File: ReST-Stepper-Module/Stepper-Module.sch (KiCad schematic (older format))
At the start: 13 parts, among them P1 CONN_02X10, P2 CONN_01X04, P3 CONN_01X04, P4 CONN_01X04, P5 CONN_01X04, P6 CONN_02X03, P7 CONN_02X03, U1 POLOLU_A4988, U2 POLOLU_A4988

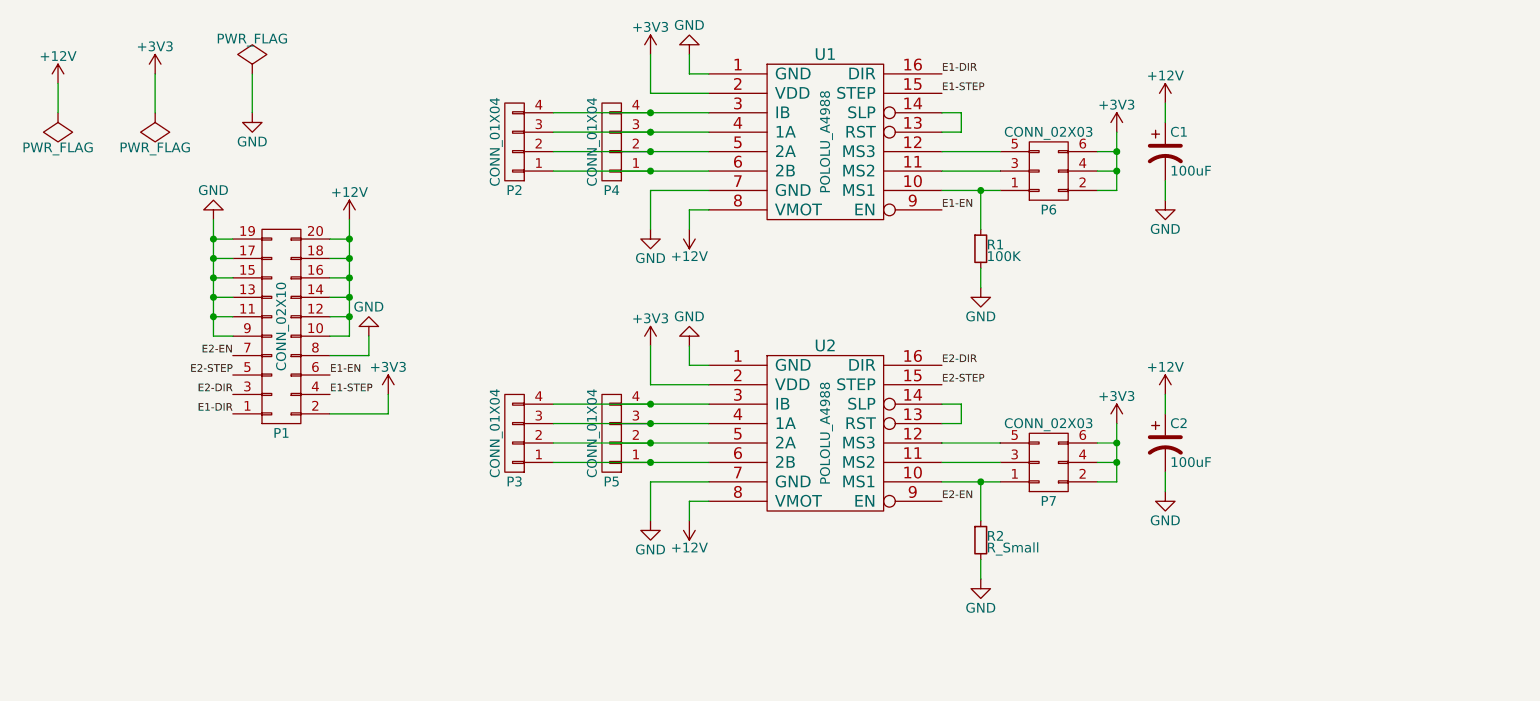
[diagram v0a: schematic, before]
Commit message: Added Images and PDF's
+ Silkscreening
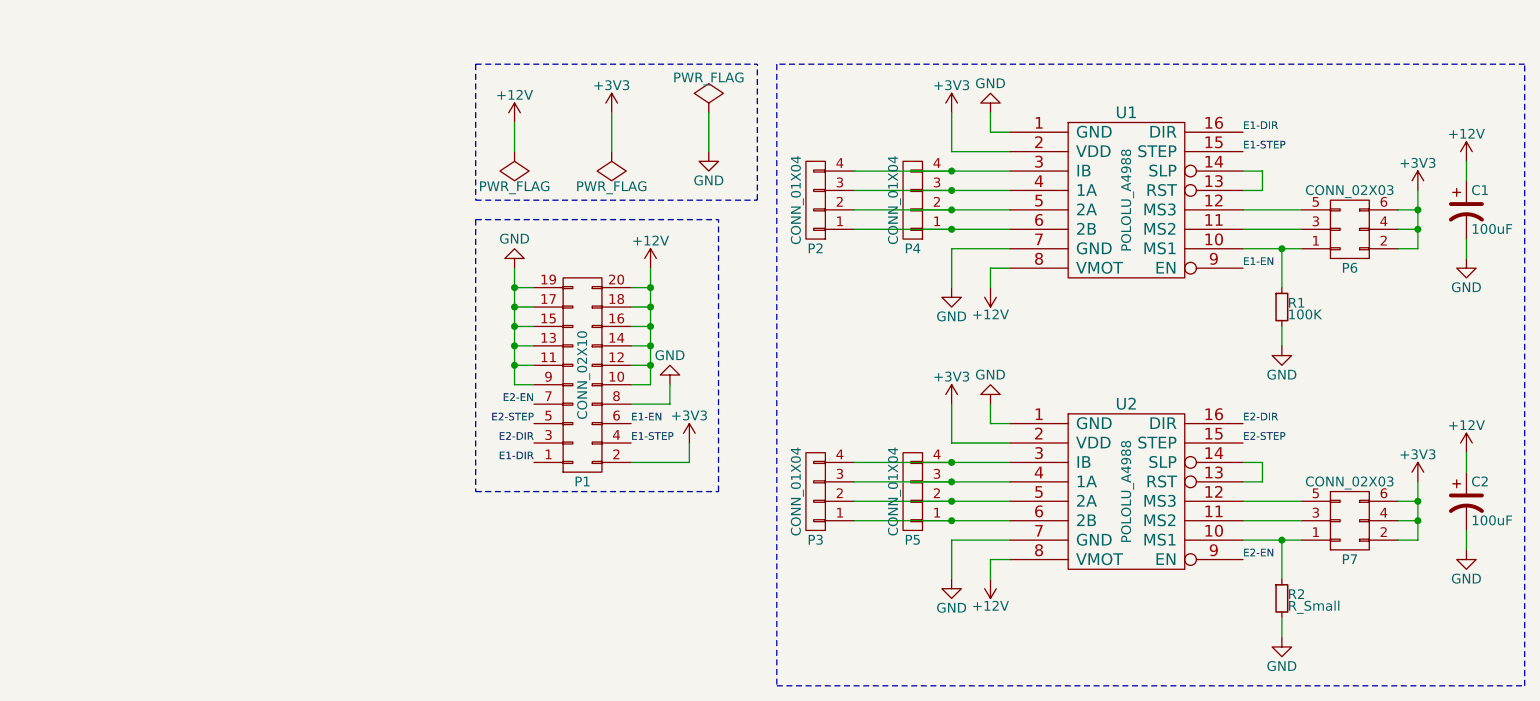
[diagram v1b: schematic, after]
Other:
- moved on the sheet: C1, C2, P1, P2, P3, P4, P5, P6, P7, R1, R2, U1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

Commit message: Finally removed all unnecessary Libs and added Heatsink for 5V Regulator
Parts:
- C1, C2: footprint ok-polcaps-panasonic:CP-PANASONIC-SMT_D8 -> ReST-Library:CP-PANASONIC-SMT_D8
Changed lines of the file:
@@
 F 0 "C1" H 8525 3150 50  0000 L CNN
 F 1 "100uF" H 8525 2950 50  0000 L CNN
-F 2 "ok-polcaps-panasonic:CP-PANASONIC-SMT_D8" H 8500 3050 50  0001 C CNN
+F 2 "ReST-Library:CP-PANASONIC-SMT_D8" H 8500 3050 50  0001 C CNN
 F 3 "" H 8500 3050 50  0000 C CNN
 	1    8500 3050
@@
 F 0 "C2" H 8525 4650 50  0000 L CNN
 F 1 "100uF" H 8525 4450 50  0000 L CNN
-F 2 "ok-polcaps-panasonic:CP-PANASONIC-SMT_D8" H 8500 4550 50  0001 C CNN
+F 2 "ReST-Library:CP-PANASONIC-SMT_D8" H 8500 4550 50  0001 C CNN
 F 3 "" H 8500 4550 50  0000 C CNN
 	1    8500 4550

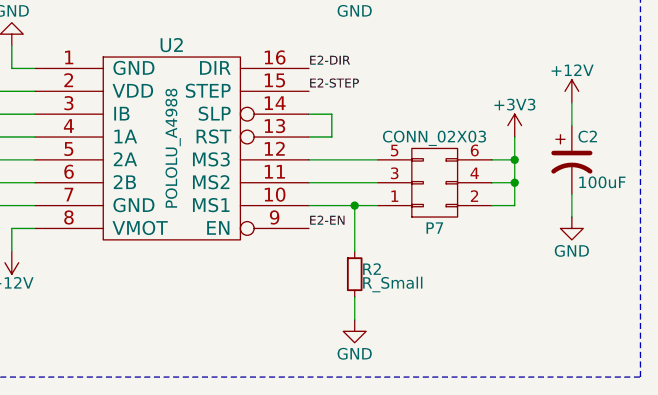
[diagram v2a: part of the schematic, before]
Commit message: Added BOM for all Items + suggested Links
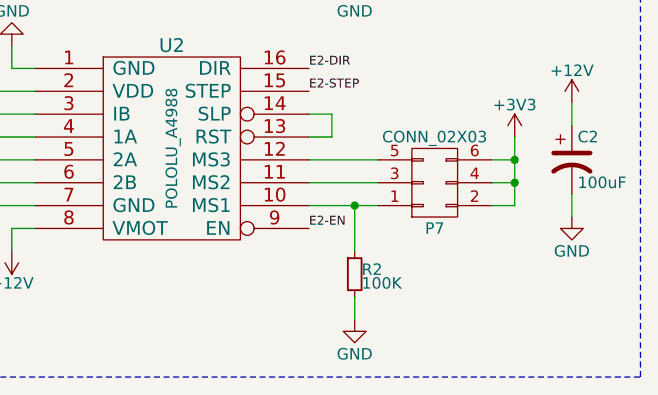
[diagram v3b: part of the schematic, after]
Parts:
- R2: value R_Small -> 100K
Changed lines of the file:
@@
 P 7550 5050
 F 0 "R2" H 7580 5070 50  0000 L CNN
-F 1 "R_Small" H 7580 5010 50  0000 L CNN
+F 1 "100K" H 7580 5010 50  0000 L CNN
 F 2 "Resistors_SMD:R_0805_HandSoldering" H 7550 5050 50  0001 C CNN
 F 3 "" H 7550 5050 50  0000 C CNN

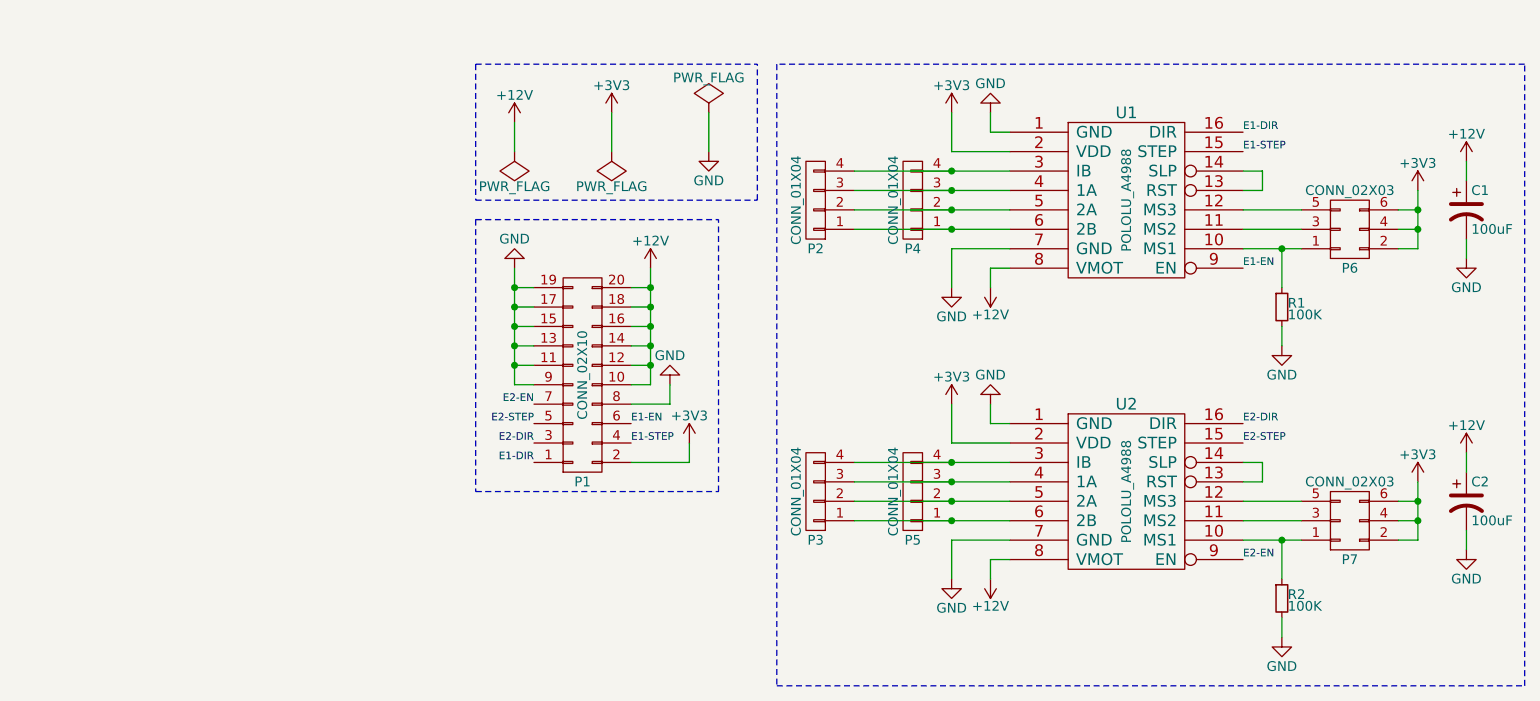
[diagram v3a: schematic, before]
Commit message: Reworked Modules to sit ontop of the mainboard
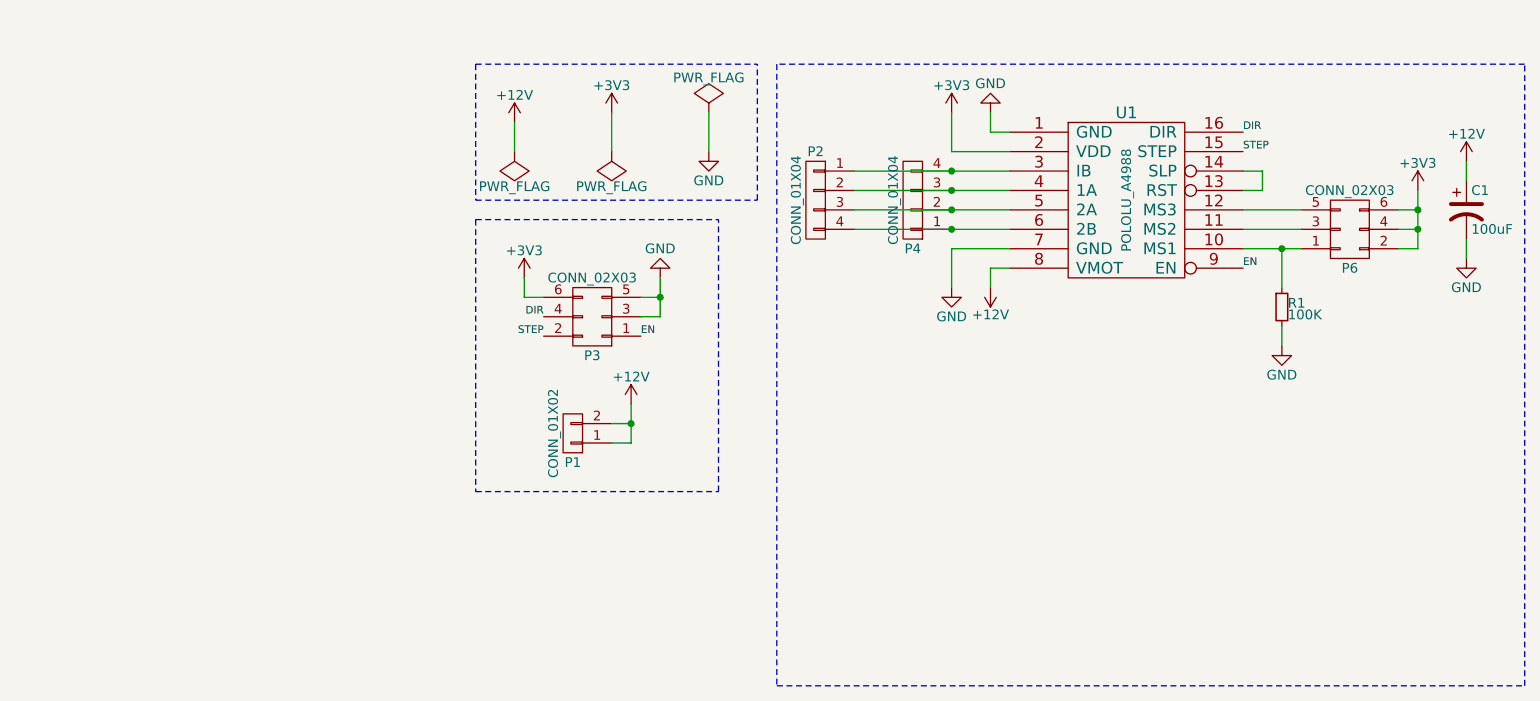
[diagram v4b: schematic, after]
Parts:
- removed C2: 100uF, ReST-Library:CP-PANASONIC-SMT_D8, symbol CP1
- removed P1: CONN_02X10, Pin_Headers:Pin_Header_Angled_2x10, symbol CONN_02X10
- removed P3: CONN_01X04, 2:mpt_0,5%2f4-2,54, symbol CONN_01X04
- removed P5: CONN_01X04, Pin_Headers:Pin_Header_Straight_1x04, symbol CONN_01X04
- removed P7: CONN_02X03, Pin_Headers:Pin_Header_Straight_2x03, symbol CONN_02X03
- removed R2: 100K, Resistors_SMD:R_0805_HandSoldering, symbol R_Small
- removed U2: POLOLU_A4988, ReST-Library:SWDIP8_.6W, symbol POLOLU_A4988
- added P1: CONN_01X02, ReST-Library:bb02-hy02a, symbol CONN_01X02
- added P3: CONN_02X03, ReST-Library:bb02-hp06, symbol CONN_02X03
- P2: footprint 2:mpt_0,5%2f4-2,54 -> ReST-Library:pt_1,5-4-3,5-h
- P6: footprint Pin_Headers:Pin_Header_Straight_2x03 -> ReST-Library:bb02-hp06
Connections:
- net +12V: now also P1.1 (P1), P1.2 (P2)
- net +3V3: now also P3.6 (P6)
- net GND: now also P3.3 (P3), P3.5 (P5)
- net at P4.4 (P4), U1.3 (IB): now also P2.1 (P1); no longer P2.4 (P4)
- net at P4.3 (P3), U1.4 (1A): now also P2.2 (P2); no longer P2.3 (P3)
- net at P4.2 (P2), U1.5 (2A): now also P2.3 (P3); no longer P2.2 (P2)
- net at P4.1 (P1), U1.6 (2B): now also P2.4 (P4); no longer P2.1 (P1)
- net E1-DIR renamed DIR
- net DIR: now also P3.4 (P4)
- net E1-EN renamed EN
- net EN: now also P3.1 (P1)
- net E1-STEP renamed STEP
- net STEP: now also P3.2 (P2)
